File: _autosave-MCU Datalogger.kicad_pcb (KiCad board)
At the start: 2 copper layers, 50.8 x 30.5 mm, 29 parts, among them J1 Conn_01x09_Pin, J2 Conn_01x04_Pin, J3 Conn_01x04_Pin, J4 Conn_02x03_Odd_Even, U1 24LC1025, U2 DS1337S_, U3 24LC1025, U4 ATMEGA328P-AU, Y1 32.768 KHz, Y2 16MHz

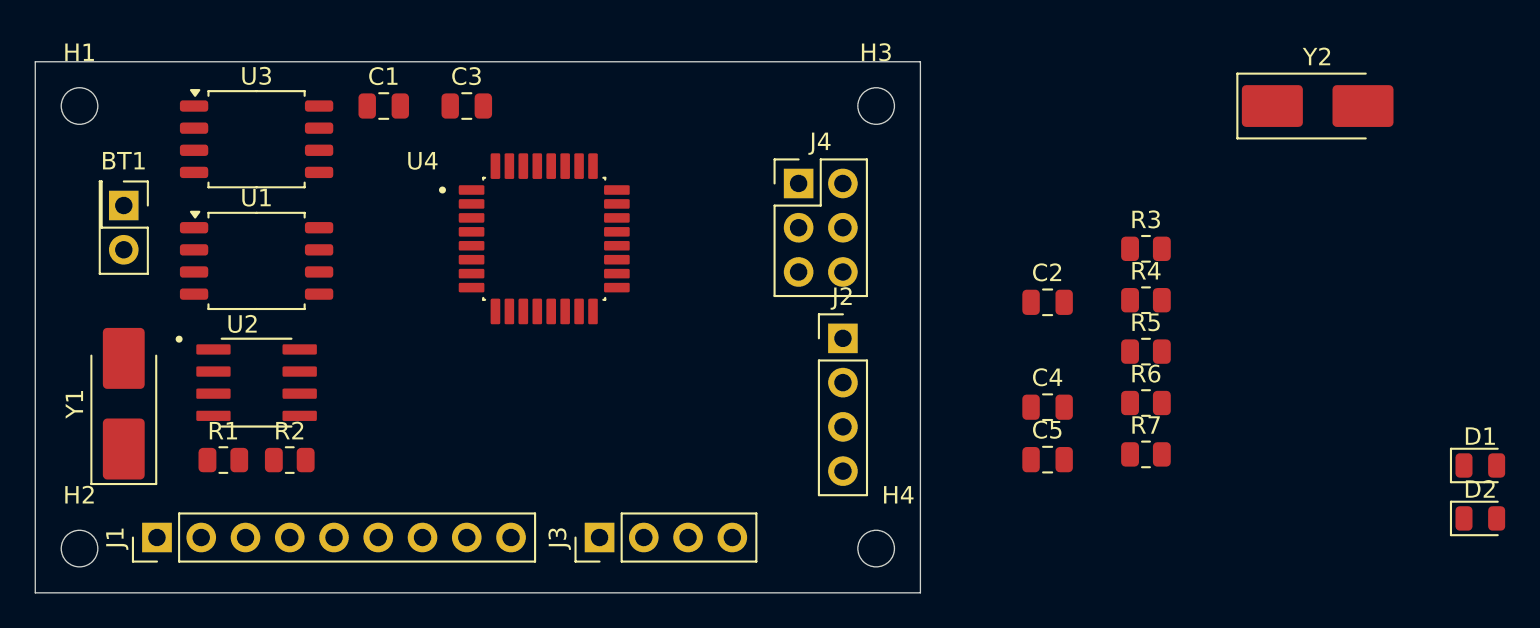
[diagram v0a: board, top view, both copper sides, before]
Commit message: Refined and completed outline
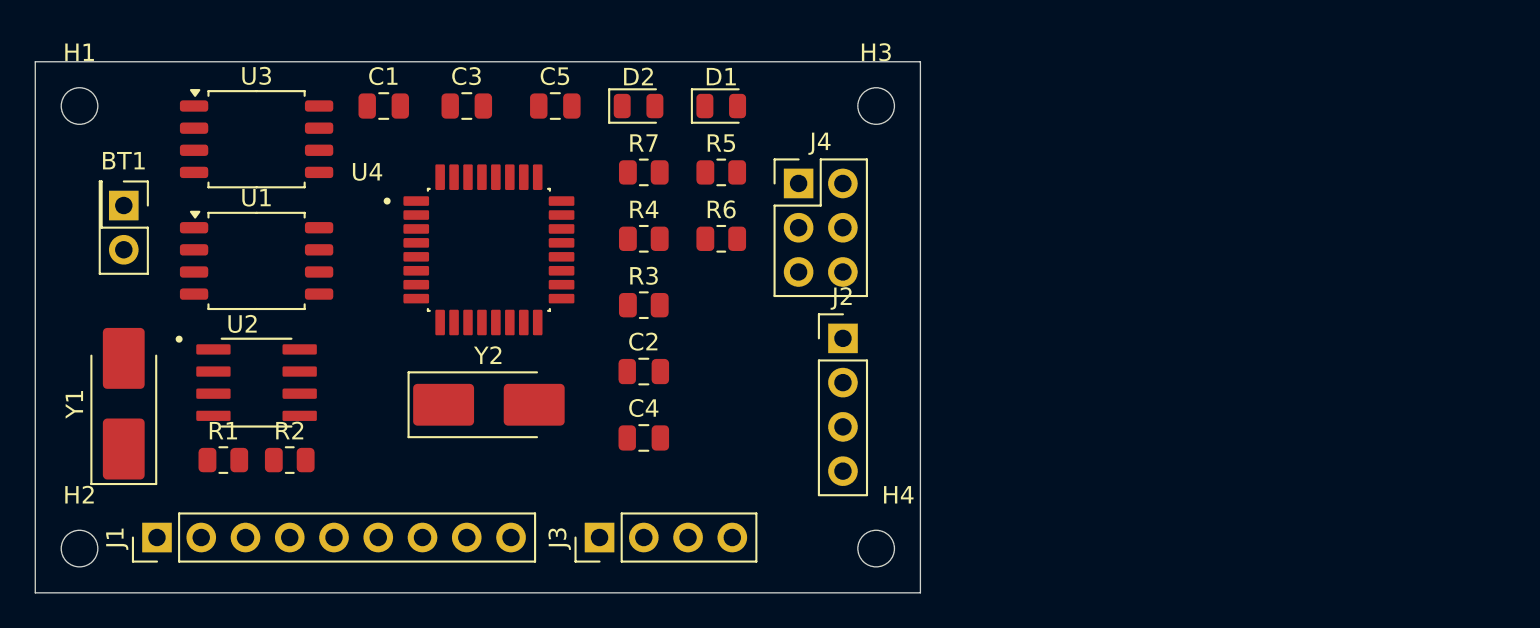
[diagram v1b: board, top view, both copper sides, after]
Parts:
- moved D2 53.8 mm to (121.0, 59.7)
- moved Y2 50.6 mm to (112.4, 76.8)
- moved D1 48.2 mm to (125.7, 59.7)
- moved C5 34.8 mm to (116.2, 59.7)
- moved R7 33.1 mm to (121.3, 63.5)
- moved R4 29.0 mm to (121.3, 67.3)
- moved R3 29.0 mm to (121.3, 71.1)
- moved R5 26.5 mm to (125.7, 63.5)
- moved R6 26.1 mm to (125.7, 67.3)
- moved C2 23.5 mm to (121.3, 74.9)
- moved C4 23.2 mm to (121.3, 78.7)
- moved U4 3.24 mm to (112.4, 67.9)
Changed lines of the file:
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@@
 	(footprint "LED_SMD:LED_0805_2012Metric"
 		(layer "F.Cu")
-		(at 169.295 80.32)
+		(at 125.73 59.69)
 		(descr "LED SMD 0805 (2012 Metric), square (rectangular) end terminal, IPC-7351 nominal, (Body size source: https://docs.google.com/spreadsheets/d/1BsfQQcO9C6DZCsRaXUlFlo91Tg2WpOkGARC1WS5S8t0/edit?usp=sharing), generated with kicad-footprint-generator")
 		(tags "LED")
@@
 	(footprint "Crystal:Crystal_SMD_5032-2Pin_5.0x3.2mm_HandSoldering"
 		(layer "F.Cu")
-		(at 159.96 59.69)
+		(at 112.395 76.835)
 		(descr "SMD2520/2, Crystal, 5.0x3.2mm package, SMD, hand-soldering, generated with kicad-footprint-generator make_crystal.py, http://www.icbase.com/File/PDF/HKC/HKC00061008.pdf")
 		(property "Reference" "Y2"
@@
 	(footprint "Resistor_SMD:R_0805_2012Metric"
 		(layer "F.Cu")
-		(at 150.105 76.735)
+		(at 125.73 67.31)
 		(descr "Resistor SMD 0805 (2012 Metric), square (rectangular) end terminal, IPC-7351 nominal, (Body size source: IPC-SM-782 page 72, https://www.pcb-3d.com/wordpress/wp-content/uploads/ipc-sm-782a_amendment_1_and_2.pdf), generated with kicad-footprint-generator")
 		(tags "resistor")
@@
 	(footprint "Resistor_SMD:R_0805_2012Metric"
 		(layer "F.Cu")
-		(at 150.105 73.785)
+		(at 125.73 63.5)
 		(descr "Resistor SMD 0805 (2012 Metric), square (rectangular) end terminal, IPC-7351 nominal, (Body size source: IPC-SM-782 page 72, https://www.pcb-3d.com/wordpress/wp-content/uploads/ipc-sm-782a_amendment_1_and_2.pdf), generated with kicad-footprint-generator")
 		(tags "resistor")
@@
 	(footprint "Resistor_SMD:R_0805_2012Metric"
 		(layer "F.Cu")
-		(at 150.105 70.835)
+		(at 121.285 67.31)
 		(descr "Resistor SMD 0805 (2012 Metric), square (rectangular) end terminal, IPC-7351 nominal, (Body size source: IPC-SM-782 page 72, https://www.pcb-3d.com/wordpress/wp-content/uploads/ipc-sm-782a_amendment_1_and_2.pdf), generated with kicad-footprint-generator")
 		(tags "resistor")
@@
 	(footprint "LED_SMD:LED_0805_2012Metric"
 		(layer "F.Cu")
-		(at 169.295 83.36)
+		(at 120.9825 59.69)
 		(descr "LED SMD 0805 (2012 Metric), square (rectangular) end terminal, IPC-7351 nominal, (Body size source: https://docs.google.com/spreadsheets/d/1BsfQQcO9C6DZCsRaXUlFlo91Tg2WpOkGARC1WS5S8t0/edit?usp=sharing), generated with kicad-footprint-generator")
 		(tags "LED")
@@
 	(footprint "Resistor_SMD:R_0805_2012Metric"
 		(layer "F.Cu")
-		(at 150.105 67.885)
+		(at 121.285 71.12)
 		(descr "Resistor SMD 0805 (2012 Metric), square (rectangular) end terminal, IPC-7351 nominal, (Body size source: IPC-SM-782 page 72, https://www.pcb-3d.com/wordpress/wp-content/uploads/ipc-sm-782a_amendment_1_and_2.pdf), generated with kicad-footprint-generator")
 		(tags "resistor")
@@
 	(footprint "Capacitor_SMD:C_0805_2012Metric"
 		(layer "F.Cu")
-		(at 144.46 70.955)
+		(at 121.285 74.93)
 		(descr "Capacitor SMD 0805 (2012 Metric), square (rectangular) end terminal, IPC-7351 nominal, (Body size source: IPC-SM-782 page 76, https://www.pcb-3d.com/wordpress/wp-content/uploads/ipc-sm-782a_amendment_1_and_2.pdf, https://docs.google.com/spreadsheets/d/1BsfQQcO9C6DZCsRaXUlFlo91Tg2WpOkGARC1WS5S8t0/edit?usp=sharing), generated with kicad-footprint-generator")
 		(tags "capacitor")
@@
 	(footprint "Capacitor_SMD:C_0805_2012Metric"
 		(layer "F.Cu")
-		(at 144.46 76.975)
+		(at 121.285 78.74)
 		(descr "Capacitor SMD 0805 (2012 Metric), square (rectangular) end terminal, IPC-7351 nominal, (Body size source: IPC-SM-782 page 76, https://www.pcb-3d.com/wordpress/wp-content/uploads/ipc-sm-782a_amendment_1_and_2.pdf, https://docs.google.com/spreadsheets/d/1BsfQQcO9C6DZCsRaXUlFlo91Tg2WpOkGARC1WS5S8t0/edit?usp=sharing), generated with kicad-footprint-generator")
 		(tags "capacitor")
@@
 	(footprint "Resistor_SMD:R_0805_2012Metric"
 		(layer "F.Cu")
-		(at 150.105 79.685)
+		(at 121.285 63.5)
 		(descr "Resistor SMD 0805 (2012 Metric), square (rectangular) end terminal, IPC-7351 nominal, (Body size source: IPC-SM-782 page 72, https://www.pcb-3d.com/wordpress/wp-content/uploads/ipc-sm-782a_amendment_1_and_2.pdf), generated with kicad-footprint-generator")
 		(tags "resistor")
@@
 	(footprint "Capacitor_SMD:C_0805_2012Metric"
 		(layer "F.Cu")
-		(at 144.46 79.985)
+		(at 116.205 59.69)
 		(descr "Capacitor SMD 0805 (2012 Metric), square (rectangular) end terminal, IPC-7351 nominal, (Body size source: IPC-SM-782 page 76, https://www.pcb-3d.com/wordpress/wp-content/uploads/ipc-sm-782a_amendment_1_and_2.pdf, https://docs.google.com/spreadsheets/d/1BsfQQcO9C6DZCsRaXUlFlo91Tg2WpOkGARC1WS5S8t0/edit?usp=sharing), generated with kicad-footprint-generator")
 		(tags "capacitor")
@@
 	(footprint "FOOTPRINTS:ATMEGA"
 		(layer "F.Cu")
-		(at 115.57 67.31)
+		(at 112.395 67.945)
 		(property "Reference" "U4"
 			(at -6.985 -4.445 0)
@@
 		)
 		(property "Value" "ATMEGA328P-AU"
-			(at 7.365 6.79 0)
+			(at 1.27 6.35 0)
 			(layer "F.Fab")
 			(effects
